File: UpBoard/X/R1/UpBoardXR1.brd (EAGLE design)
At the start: 88.9 x 88.6 mm, 75 parts, among them CN1 100nF, CN2 100nF, CN3 100nF, CN4 100nF, IC1 SAM3X8E(ARDUINO), J1 2POSTERMINALBLOCK.25"PITCH, Q6 2N7002E, X1 16POS_RIBBON, X2 16POS_RIBBON, X3 16POS_RIBBON, X4 16POS_RIBBON, Y1 FH1200001, Y2 ABS05

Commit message: Update R1
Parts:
- added RST_EN1: 1K, resistor:R0402
- US1: device adafruit:USB-MINIB -> SparkFun-Connectors:USB-B-MICRO-SMD
- moved X4 90.1 mm to (5.08, 22.6), turned to 90 degrees
- moved X1 89.9 mm to (83.8, 22.6), turned to 270 degrees
- moved X3 81.1 mm to (5.08, 53.6), turned to 90 degrees
- moved X2 81.1 mm to (83.9, 53.6), turned to 270 degrees
- moved R4 76.6 mm to (73.5, 63.1), turned to 0 degrees
- moved R17 74.6 mm to (76.6, 61.7)
- moved C5 73.3 mm to (13.8, 65.3)
- moved C4 70.7 mm to (13.8, 59.6), turned to 0 degrees
- moved Y1 69.9 mm to (13.8, 62.2), turned to 90 degrees
- moved Q6 69.0 mm to (73.4, 63.2), turned to 180 degrees
- moved C6 66.1 mm to (13.9, 57.1), turned to 180 degrees
- moved Y2 64.6 mm to (13.8, 54.6), turned to 270 degrees
- moved ERASE_EN 63.3 mm to (76.0, 36.6), turned to 0 degrees
- moved C7 63.0 mm to (13.9, 52.1), turned to 180 degrees
- moved RESET 62.7 mm to (64.9, 39.3), turned to 0 degrees
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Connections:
- removed net N$13: U$4.P1
- removed net N$14: U$4.P3
- removed net N$15: U$4.P7
- removed net N$3: U$4.P6
- net 3.3V: now also RST_EN1.1, XA1.P$2
- net D6: now also U$4.P7
- net D7: now also RST_EN1.2, U$4.P1
- net D8: now also U$4.P3
- net HV: no longer XA1.P$2, XA1.P$3
- net MISO: no longer U$4.P5
- net MOSI: now also U$4.P5
- net SCK: now also U$4.P6
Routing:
- net 3.3V: track 4.75 -> 29.3 mm
- net D8: track 0.00 -> 22.4 mm
- net D7: track 0.00 -> 22.3 mm
- net HV: track 28.9 -> 9.50 mm
- net PS1-1:BATT_5V: track 19.8 -> 4.19 mm
- net D6: track 0.00 -> 11.9 mm
- net PS1-1:USB_FILTERED: track 13.9 -> 22.7 mm, vias 0 -> 2
- net N$10: track 0.00 -> 5.40 mm
- net N$7: track 0.00 -> 5.32 mm
- net 5V: track 4.46 -> 0.00 mm
- net PS1-1:N$2: track 11.4 -> 15.3 mm
- net N$8: track 0.00 -> 3.79 mm
- net N$38: track 0.00 -> 3.66 mm
- net N$32: track 5.38 -> 8.53 mm
- net N$34: track 4.43 -> 7.05 mm
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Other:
- board size 88.9 x 88.6 mm -> 88.9 x 76.2 mm
- board text added: "R1"

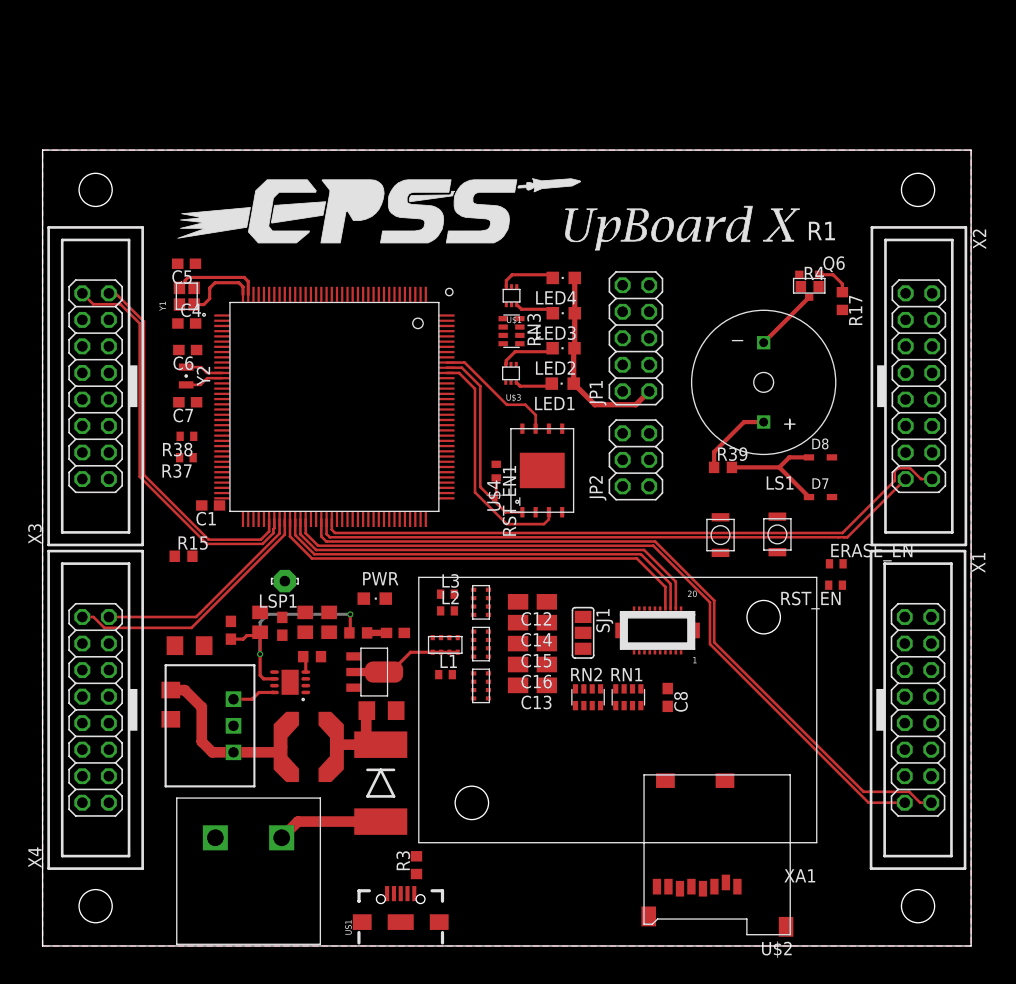
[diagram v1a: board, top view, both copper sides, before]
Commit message: Connected Flash corrctly, changed sheet size
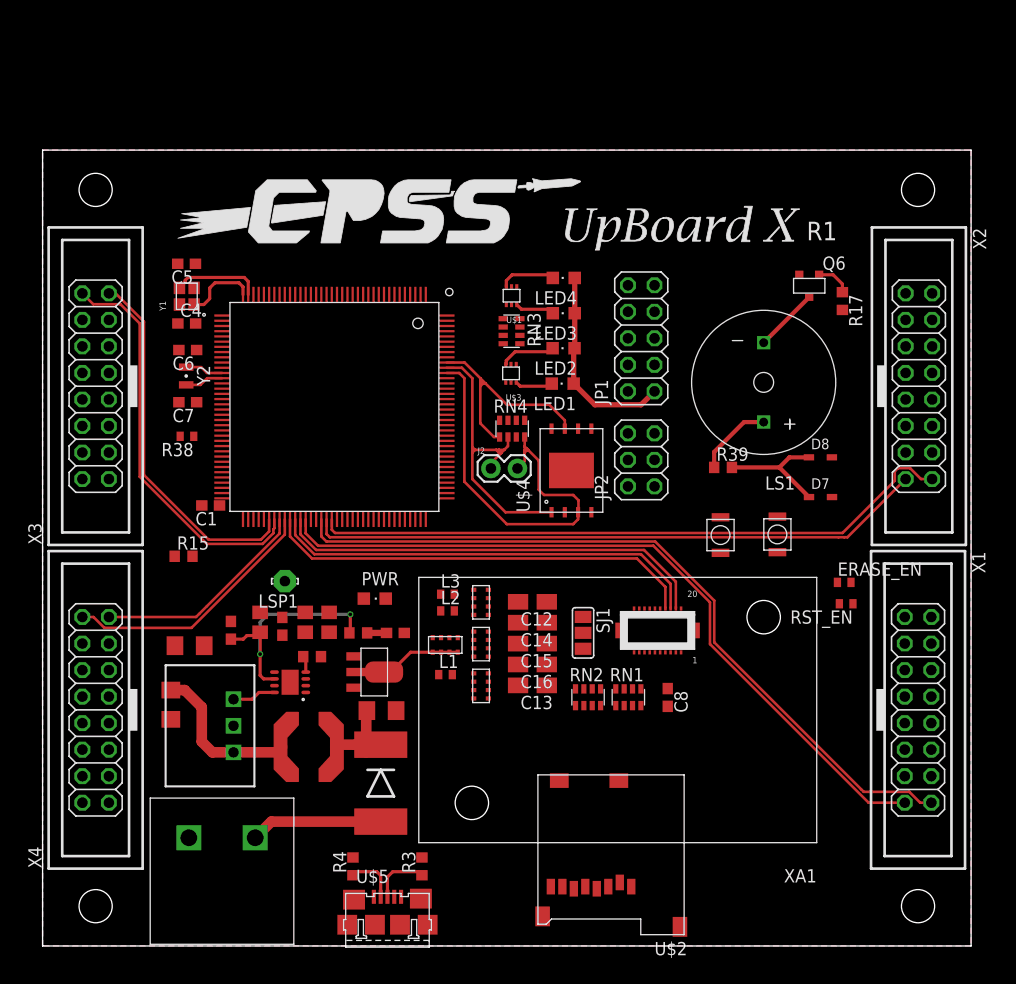
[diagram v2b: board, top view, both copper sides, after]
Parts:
- removed R37: 0R, resistor:R0402
- removed RST_EN1: 1K, resistor:R0402
- removed US1: (no value), SparkFun-Connectors:USB-B-MICRO-SMD
- added J2: (no value), SparkFun-Connectors:1X02
- added RN4: 1K, resistor-net:CTS742C083
- added U$5: MICROUSB_5POS_SMT, CPSS_CONNECTOR:RECPT_SMT_R/A
- R38: value 0R -> 220R
- moved R4 70.7 mm to (29.7, 7.62), turned to 90 degrees
- moved U$2 10.2 mm to (61.7, 16.4)
- moved U$4 2.79 mm to (50.6, 45.5)
- moved J1 2.54 mm to (17.2, 10.4)
- moved RST_EN 2.05 mm to (76.9, 32.8)
- moved ERASE_EN 1.93 mm to (76.8, 34.8)
- moved R3 0.54 mm to (36.3, 7.62)
- moved JP1 0.51 mm to (57.3, 58.2)
- moved JP2 0.51 mm to (57.3, 46.5)
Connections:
- net 3.3V: now also RN4.7, RN4.8; no longer RST_EN1.1
- net D+: now also U$5.P3; no longer US1.D+
- net D-: now also U$5.P2; no longer US1.D-
- net D6: now also RN4.1
- net D7: now also J2.1, RN4.2; no longer RST_EN1.2
- net D8: now also J2.2, RN4.4
- net GND: now also RN4.5, U$5.P5; no longer R37.2, US1.GND
- net TST: no longer R37.1
- net UOTGID: now also U$5.P4; no longer US1.ID
- net VBUS: now also U$5.P1; no longer US1.VBUS
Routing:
- net D8: track 22.4 -> 39.8 mm
- net D6: track 11.9 -> 22.3 mm
- net D7: track 22.3 -> 30.0 mm
- net D+: track 0.00 -> 5.55 mm
- net D-: track 0.00 -> 4.98 mm
- net N$4: track 10.1 -> 12.7 mm
- net 3.3V: track 29.3 -> 29.8 mm

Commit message: Finished routing traces, front silkscreen.
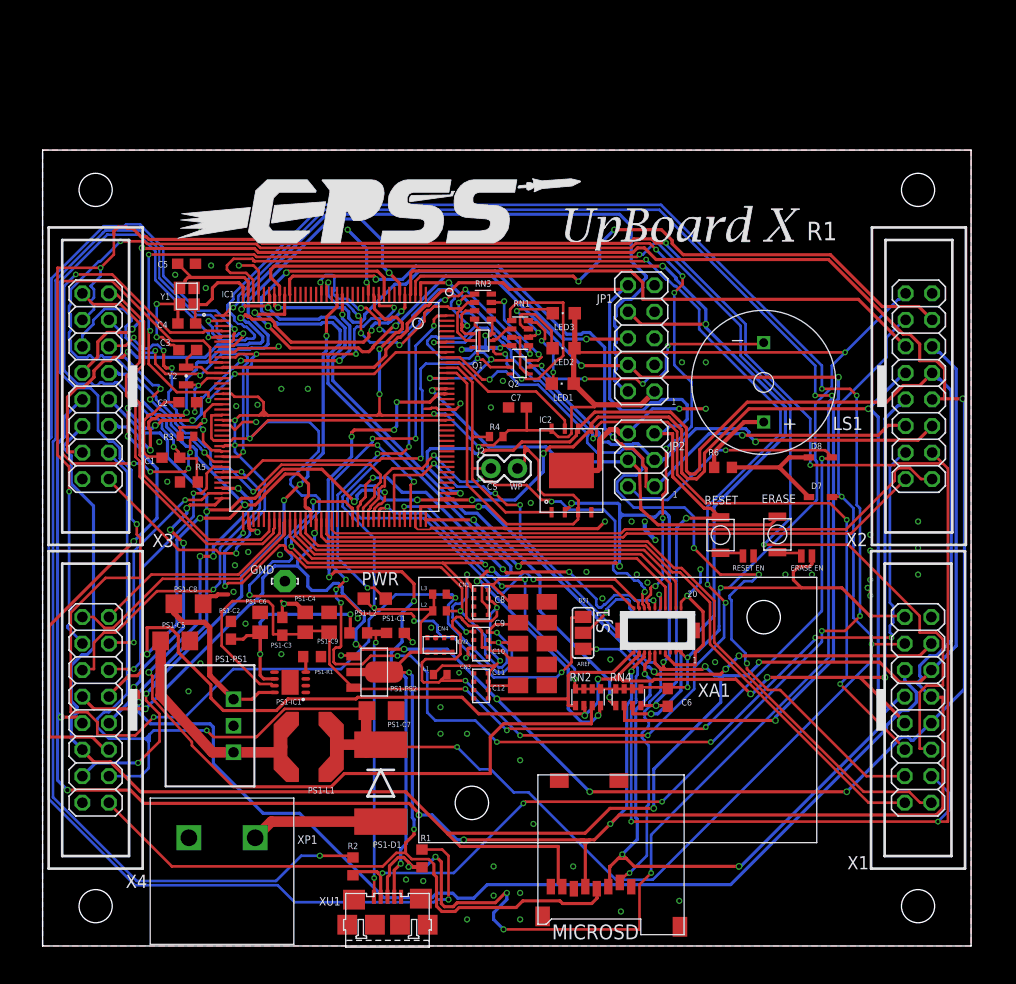
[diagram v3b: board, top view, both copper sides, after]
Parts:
- removed C13: 10uF, resistor:A/3216-18R
- removed ERASE_EN, RST_EN: 0R, resistor:R0402
- removed LED4: (no value), led:CHIPLED_0805
- removed PS1-1:C17: 100uF, resistor:C0805
- removed Q6: 2N7002E, UpBoard B:NMINI3-R1-B
- removed R15: 6.8K, resistor:R0603
- removed R17: 10k, resistor:R0603
- removed R38: 220R, resistor:R0402
- removed U$1, U$3: BC857BV-7, CPSS_IC:SOT-563
- added C2, C3: 22pF, resistor:C0603
- added PS1-1:C8: 10uF, eagle-ltspice:C1206
- added Q1, Q2: MBT3904DW2T1, CPSS_IC:SOT-363
- added R1, R2: 39, resistor:R0603
- added R5: 6.8K, resistor:R0603
- added U$6, U$7: SOLBRDG, CPSS_CONNECTOR:SOLBRDG
- C6: value 22pF -> 10n
- C7: value 22pF -> 100n
- C8: value 10n -> 10uF; device resistor:C0603 -> resistor:A/3216-18R
- PS1-1:C1: value 10uF -> 10nF; device eagle-ltspice:C1206 -> eagle-ltspice:C0603
- PS1-1:C2: value 10uF -> 100nF; device eagle-ltspice:C1206 -> eagle-ltspice:C0603
- PS1-1:C3: value 4.7uF -> 100nF; device eagle-ltspice:C1206 -> resistor:C0603
- PS1-1:C4: value 10nF -> 1uF; device eagle-ltspice:C0603 -> eagle-ltspice:C0805
- PS1-1:C5: value 100nF -> 4.7uF; device eagle-ltspice:C0603 -> eagle-ltspice:C1206
- PS1-1:C7: value (none) -> 10uF; device eagle-ltspice:C0805 -> eagle-ltspice:C1206
- PS1-1:C9: value 100nF -> 100uF; device resistor:C0603 -> resistor:C0805
- R3, R4: value 39 -> 220R; device resistor:R0603 -> resistor:R0402
- RN1: value 10K -> 65R
- RN2: value 1k -> 4.7K
- RN3: value 10K -> 100K
- RN4: value 1K -> 100K
- moved C6 56.7 mm to (59.9, 23.8), turned to 270 degrees
- moved R3 46.9 mm to (13.8, 48.8), turned to 180 degrees
- moved R4 43.4 mm to (43.4, 48.8), turned to 0 degrees
- moved RN1 36.4 mm to (45.7, 58.7), turned to 90 degrees
- moved C7 31.6 mm to (45.5, 51.6), turned to 0 degrees
- moved RN4 28.0 mm to (56.1, 23.8)
- moved C8 15.9 mm to (46.9, 33.0), turned to 180 degrees
- moved PS1-1:C3 13.1 mm to (23.0, 30.6), turned to 90 degrees
- moved PS1-1:C7 11.2 mm to (32.4, 22.5), turned to 0 degrees
- moved PS1-1:C4 8.70 mm to (25.1, 31.0), turned to 90 degrees
- moved C12 8.00 mm to (46.9, 24.9)
- moved CN3 8.00 mm to (42.0, 24.9)
- moved PS1-1:C1 7.56 mm to (33.8, 30.0)
- moved C1 5.95 mm to (12.3, 46.7)
- moved PS1-1:C5 5.43 mm to (12.7, 29.2), turned to 0 degrees
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- renumbered C14 to C9, C15 to C10, C16 to C11, J1 to XP1, LSP1 to GND, PS1-1:U$1 to PS1-1:PS1, PS1-1:U$2 to PS1-1:IC1, PS1-1:U$3 to PS1-1:D1, R39 to R6, U$4 to IC2, U$5 to XU1
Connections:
- net N$17 renamed D26
- removed net N$38: LED1.C, U$3.C1
- removed net N$8: LED3.C, U$1.C1
- new net N$1: LED3.C, RN1.2
- new net N$11: Q1.P$5, RN1.6
- new net N$12: Q1.P$4, RN1.5
- new net N$3: LED2.C, RN1.3
- new net N$5: PWR.C, RN1.1
- net 1.8V: now also C12.+, CN1.P$1, CN1.P$2, CN3.P$3, CN3.P$4; no longer C13.+, CN2.P$1, CN2.P$2, CN2.P$3, CN2.P$4
- net 3.3V: now also C6.1, C7.2, C8.+, CN1.P$3, CN1.P$4, R4.2, RN4.5, RN4.6, U$6.P$2; no longer C12.+, C8.1, CN3.P$3, CN3.P$4, ERASE_EN.2, LED4.A, RN1.5, RN1.6, RN1.7, RN1.8
- net 5V: now also PS1-1:C3.1, PS1-1:C4.1; no longer PS1-1:C17.1, PS1-1:C7.1
- net D+: now also R1.1; no longer R3.1
- net D-: now also R2.1; no longer R4.1
- net D10: now also U$2.2; no longer RN3.1, U$1.B2
- net D11: now also Q1.P$2; no longer U$1.B1, U$2.2
- net D12: now also Q1.P$1; no longer U$3.B2
- net D13: now also Q2.P$2; no longer U$3.B1
- net D6: no longer RN4.1
- net D7: now also R4.1; no longer RN4.2
- net D8: no longer RN4.4
- net D9: now also Q2.P$1, RN3.1; no longer Q6.1, R17.1
- net GND: now also C2.2, C3.2, C7.1, C8.-, CN1.P$5, CN1.P$6, CN1.P$7, CN1.P$8, CN2.P$2, CN2.P$3, CN2.P$4, PS1-1:C8.2, Q1.P$3, Q1.P$6, Q2.P$3, Q2.P$6, R3.2, R5.1, RN1.8, U$7.P$2; no longer C13.-, C6.2, C7.2, CN1.P$2, CN1.P$3, CN1.P$4, CN2.P$5, CN2.P$6, CN2.P$7, CN2.P$8, PS1-1:C17.2, PWR.C, Q6.2, R15.1, R17.2, R38.2, RN4.5, RST_EN.2, U$1.E1, U$1.E2, U$3.E1, U$3.E2
- net HV: now also PS1-1:C7.1; no longer PS1-1:C1.1
- net JTAG_SEL: now also R3.1; no longer R38.1
- net JTAG_TCK: now also RN4.2; no longer RN1.2
- net JTAG_TDI: now also RN4.3; no longer RN1.3
- net JTAG_TMS: now also RN4.1; no longer RN1.1
- net M_RESET: now also C6.2, RN4.4; no longer C8.2, RN1.4
- net N$10: now also Q2.P$4, RN1.7; no longer LED4.C, U$1.C2
- net N$2: now also R1.2; no longer R3.2
- net N$22: now also U$6.P$1; no longer ERASE_EN.1
- net N$33: now also Q2.P$5; no longer Q6.3
- net N$35: now also C2.1; no longer C7.1
- net N$36: now also C3.1; no longer C6.1
- net N$41: now also R5.2; no longer R15.2
- net N$6: now also U$7.P$1; no longer RST_EN.1
- net N$7: now also LED1.C, RN1.4; no longer LED2.C, U$3.C2
- net N$9: now also R2.2; no longer R4.2
- net PS1-1:BATT_5V: now also PS1-1:C8.1; no longer PS1-1:C2.1
- net PS1-1:N$2: now also PS1-1:C5.1; no longer PS1-1:C3.1
- net PS1-1:USB_FILTERED: now also PS1-1:C2.1; no longer PS1-1:C5.1
- net VBUS: now also PS1-1:C1.1; no longer PS1-1:C4.1
- net VDDANA: now also CN2.P$7; no longer CN1.P$7
- net VDDPLL: now also CN2.P$6; no longer CN1.P$6
- net VDDUTMI: now also CN2.P$8; no longer CN1.P$8
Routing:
- net 3.3V: track 29.8 -> 386.8 mm, vias 0 -> 18
- net SCK: track 0.00 -> 266.7 mm, vias 0 -> 8
- net SCL: track 0.00 -> 264.2 mm, vias 0 -> 10
- net MISO: track 0.00 -> 242.0 mm, vias 0 -> 8
- net AREF: track 0.00 -> 238.5 mm, vias 0 -> 7
- net MOSI: track 0.00 -> 216.5 mm, vias 0 -> 9
- net SDA: track 0.00 -> 179.9 mm, vias 0 -> 8
- net HV: track 9.50 -> 176.2 mm, vias 0 -> 4
- net D+: track 5.55 -> 170.8 mm, vias 0 -> 8
- net D-: track 4.98 -> 168.5 mm, vias 0 -> 8
- net D4: track 0.00 -> 163.0 mm, vias 0 -> 6
- net D49: track 0.00 -> 146.9 mm, vias 0 -> 8
- net VDDPLL: track 0.00 -> 146.5 mm, vias 0 -> 6
- net GND: track 0.00 -> 145.9 mm, vias 0 -> 84
- net 1.8V: track 0.00 -> 143.2 mm, vias 0 -> 9
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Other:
- board text added: "1"
- board text added: "AREF"
- board text added: "CN1"
- board text added: "CN2"
- board text added: "CN3"
- board text added: "CN4"
- board text added: "CS WP"
- board text added: "D51"
- board text added: "ERASE"
- board text added: "ERASE EN"
- board text added: "IC1"
- board text added: "MICROSD"
- board text added: "PS1-C1"
- board text added: "PS1-C2"
- board text added: "PS1-C3"
- board text added: "PS1-C4"
- board text added: "PS1-C5"
- board text added: "PS1-C6"
- board text added: "PS1-C7"
- board text added: "PS1-C8"
- board text added: "PS1-C9"
- board text added: "PS1-D1"
- board text added: "PS1-IC1"
- board text added: "PS1-L1"
- board text added: "PS1-L2"
- board text added: "PS1-PS1"
- board text added: "PS1-PS2"
- board text added: "PS1-R1"
- board text added: "RESET"
- board text added: "RESET EN"
- board text added: "XP1"

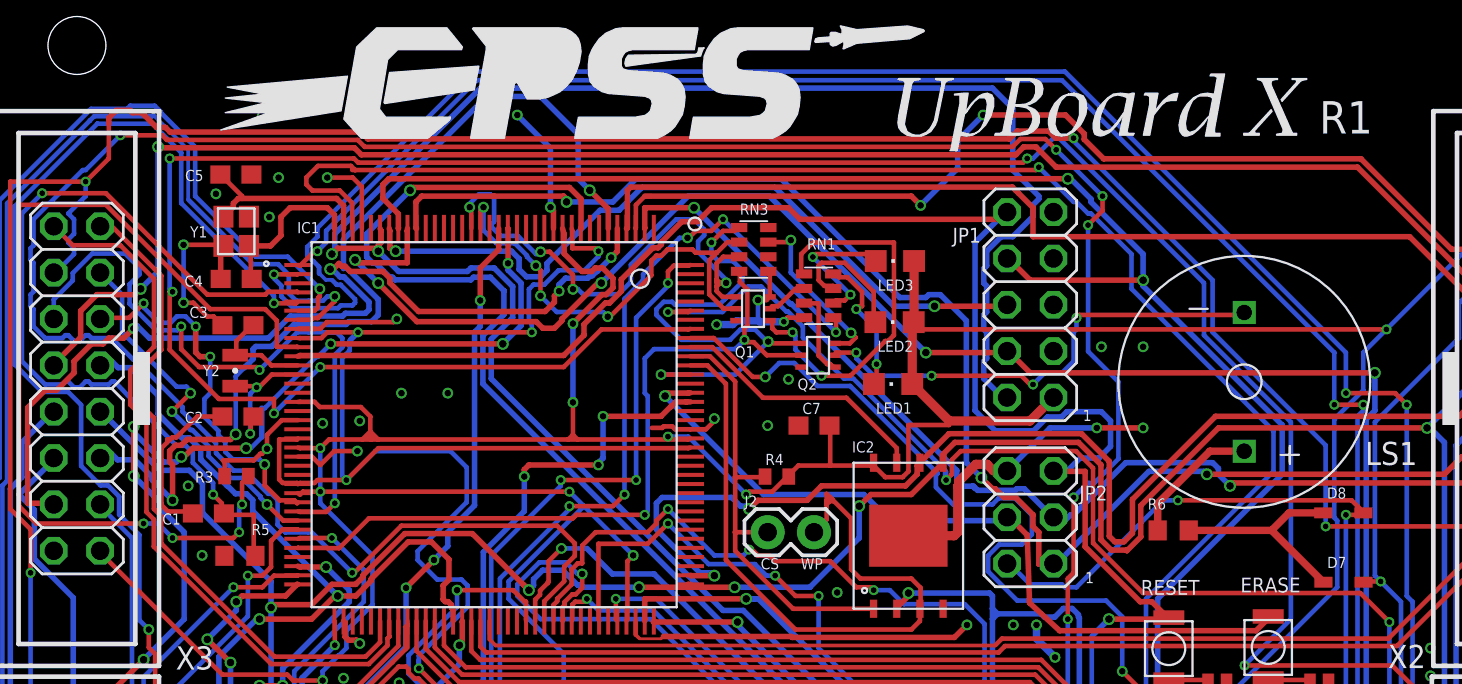
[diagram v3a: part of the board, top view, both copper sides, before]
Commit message: Fixed refdes
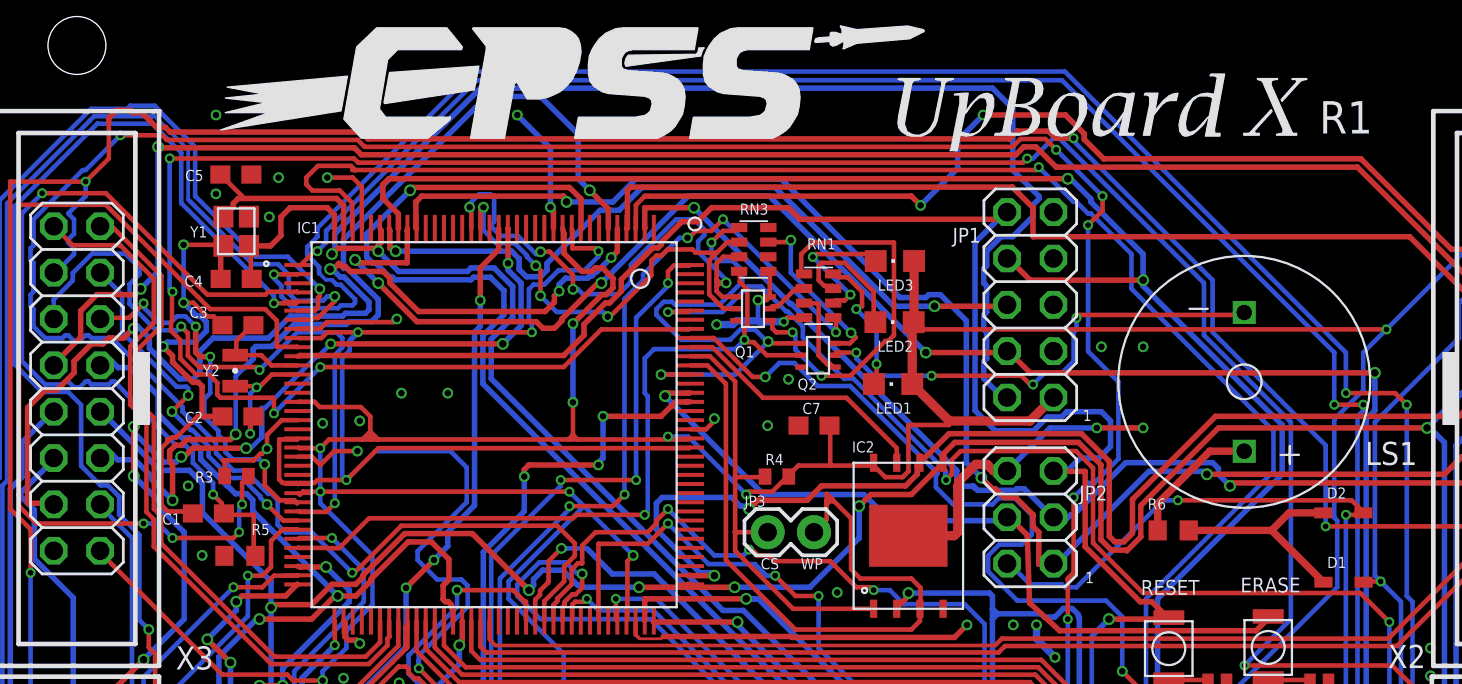
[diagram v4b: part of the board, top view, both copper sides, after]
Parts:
- renumbered D7 to D1, D8 to D2, J2 to JP3, U$2 to SD1, U$6 to SJ3, U$7 to SJ2
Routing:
- net GND: track 145.9 -> 153.5 mm, vias 84 -> 85
- net RXS1: track 52.0 -> 55.0 mm
- net D38: track 36.1 -> 37.1 mm
